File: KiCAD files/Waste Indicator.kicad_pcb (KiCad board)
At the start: 2 copper layers, 30 x 51 mm, 15 parts, among them J101 USB4500-03-0-A, J102 Conn_01x08_Socket, SW101 430172085816, U101 ESP32-S2-MINI-1, U102 AMS1117-3.3

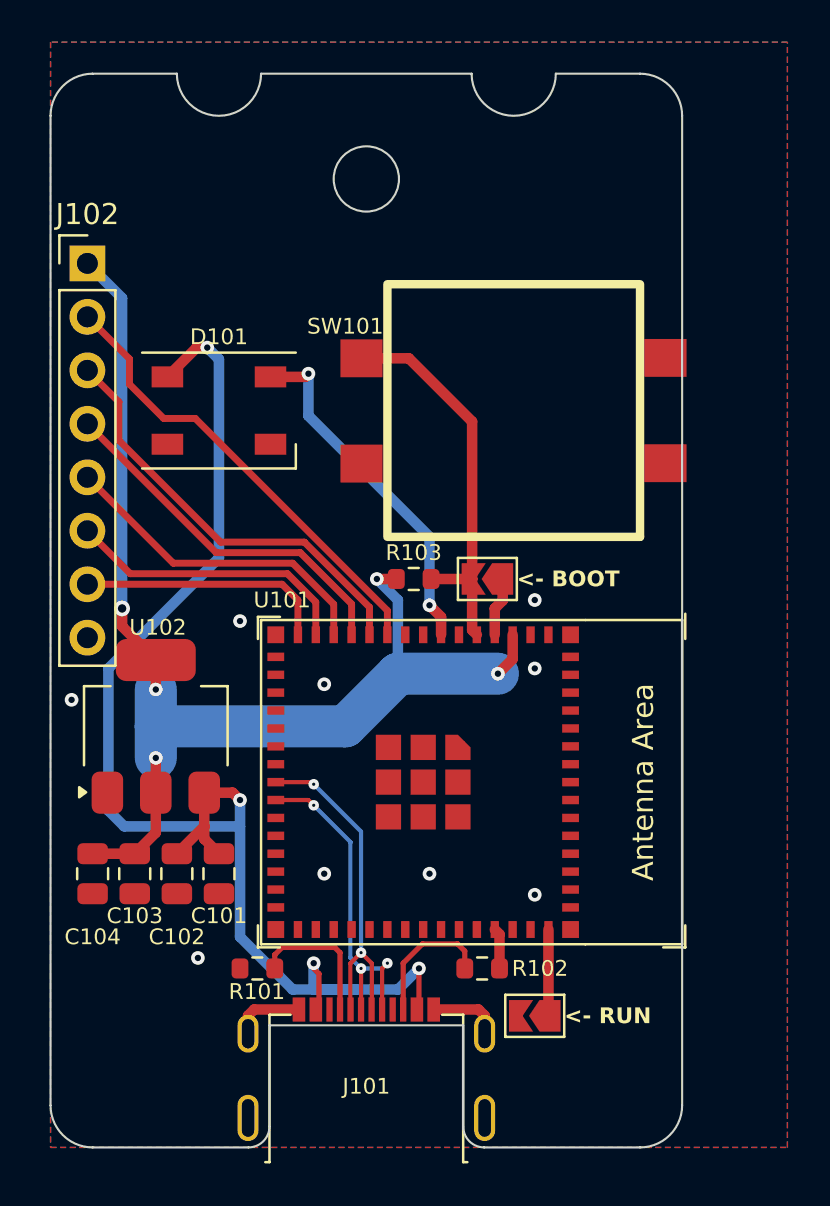
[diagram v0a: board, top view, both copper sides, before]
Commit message: Fixed PCB to V1.0
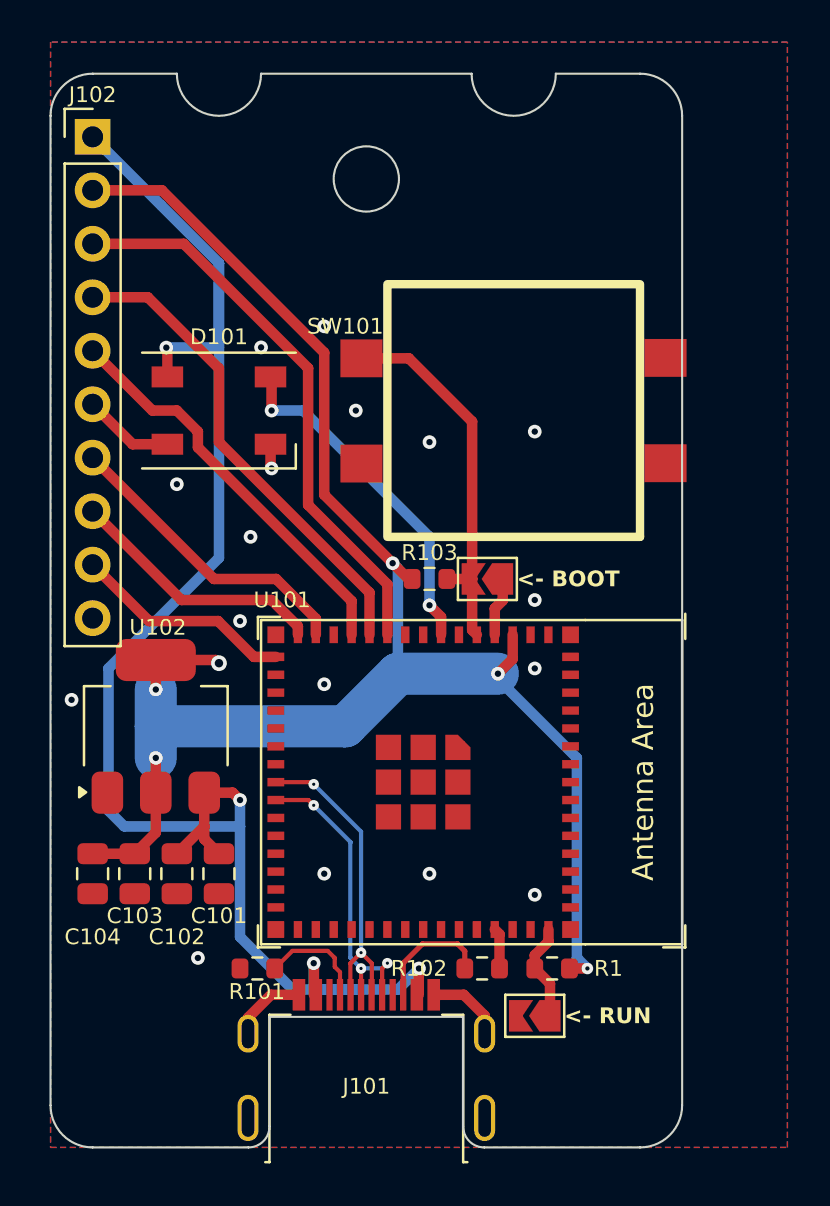
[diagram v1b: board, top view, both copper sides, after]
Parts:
- added R1: 5K1, Resistor_SMD:R_0603_1608Metric, F.Cu at (123.8, 91.5)
- J102: value Conn_01x08_Socket -> Conn_01x10_Socket; footprint Connector_PinHeader_2.54mm:PinHeader_1x08_P2.54mm_Vertical -> Connector_PinHeader_2.54mm:PinHeader_1x10_P2.54mm_Vertical
- moved J102 6.02 mm to (102.0, 52.0)
- moved R103 0.75 mm to (118.0, 73.0)
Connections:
- D101 pad 4: unconnected-(D101-DOUT-Pad4) -> D_{OUT}
- J102 pad 1: +3.3V -> +5V
- J102 pad 2: Net-(J102-Pin_2) -> +3.3V
- J102 pad 6: Net-(J102-Pin_6) -> D_{OUT}
- J102 pad 8: GND -> Net-(J102-Pin_8)
- U101 pad 10: Net-(J102-Pin_2) -> Net-(J102-Pin_3)
- U101 pad 11: Net-(J102-Pin_3) -> Net-(J102-Pin_4)
- U101 pad 12: Net-(J102-Pin_4) -> Net-(J102-Pin_5)
- U101 pad 13: Net-(J102-Pin_5) -> unconnected-(U101-GPIO9/ADC1_CH8-Pad13)
- U101 pad 14: Net-(J102-Pin_6) -> Net-(J102-Pin_7)
- U101 pad 15: Net-(J102-Pin_7) -> Net-(J102-Pin_8)
- U101 pad 16: unconnected-(U101-GPIO12/ADC2_CH1-Pad16) -> Net-(J102-Pin_9)
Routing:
- net +3.3V: track 57.2 -> 82.8 mm, vias 5 -> 6
- net Net-(J102-Pin_2): track 21.9 -> 0.00 mm
- net +5V: track 64.6 -> 80.5 mm
- net Net-(J102-Pin_6): track 13.8 -> 0.00 mm
- net Net-(J102-Pin_8): track 0.00 -> 12.4 mm
- net Net-(J102-Pin_9): track 0.00 -> 10.5 mm
- net Net-(J102-Pin_3): track 20.4 -> 26.9 mm
- net Net-(J102-Pin_4): track 17.6 -> 23.0 mm
- net D_{OUT}: track 0.00 -> 4.34 mm
- net Net-(J102-Pin_5): track 15.6 -> 19.3 mm
- net Net-(J102-Pin_7): track 12.0 -> 14.5 mm
- net GND: track 6.84 -> 9.33 mm, vias 9 -> 17
- net Net-(J101-CC1): track 6.70 -> 5.19 mm
- net D+: track 16.2 -> 14.8 mm
- net D-: track 16.6 -> 15.2 mm
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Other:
- outline, holes or cut-outs redrawn
- board text added: "+5V"
- board text added: "GPIO 12"
- board text added: "Houd de knop 8 sec ingedrukt"
- board text added: "SK6812 D_{OUT}"
- board text added: "Waste Indicator V1.0"
- board text removed: "1: 30s POWER OFF 2: AAN/UIT (6x) 3: 7^{e} keer aanlaten"
- board text removed: "GPIO 9"
- board text removed: "Waste Indicator V0.7"
